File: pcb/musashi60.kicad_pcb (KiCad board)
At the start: 2 copper layers, 175 x 135.7 mm, 81 parts, among them J1 MJ-4PP-9, U1 ProMicro_r

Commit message: update pcb
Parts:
- removed D_H5: D, foostan:D3_TH_SMD
- removed the G_LOGO_B at (79.8, 108.3)
- removed the G_LOGO_F at (79.8, 108.3)
- removed H_D2: MountingHole_Pad, foostan:1pin_conn
- removed SW_H5: SW_PUSH, foostan:CherryMX_Choc_Hotswap
- added G_LOGO_B: LOGO, local:musashi60-silk-256, B.Cu at (90.7, 107.0)
- added G_LOGO_F: LOGO, local:musashi60-silk-256, F.Cu at (89.5, 107.0)
- added SW_RST2: SW_PUSH, foostan:ResetSW_4P, F.Cu at (17.0, 47.6)
- moved JP_RIGHT 128.9 mm to (148.0, 18.0)
- moved JP_LEFT 125.9 mm to (148.0, 18.0)
- moved GND 33.9 mm to (25.4, 48.3)
- moved F5 30.6 mm to (25.4, 45.7)
- moved F4 27.3 mm to (25.4, 43.2)
- moved D3 23.4 mm to (25.4, 40.6)
- moved VCC 20.5 mm to (25.4, 38.1)
- moved D_G5 14.4 mm to (57.5, 119.5), turned to 10 degrees
- moved SW_G5 13.6 mm to (55.8, 110.1), turned to 10 degrees
- moved D_H4 12.4 mm to (36.2, 108.3), turned to 15 degrees
- moved D_G4 11.7 mm to (54.2, 100.7), turned to 10 degrees
- moved D_B1 11.4 mm to (149.5, 42.3)
- moved D_A3 11.3 mm to (168.5, 84.6)
- moved D_F4 11.3 mm to (73.2, 94.8), turned to 5 degrees
- moved D_A4 11.2 mm to (168.4, 103.6)
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- renumbered H_D3 to D3, H_F4 to F4, H_F5 to F5, H_GND1 to GND, H_VCC1 to VCC
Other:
- board size 175 x 135.7 mm -> 185 x 135 mm
- board text added: "Designed by @hamano"
- board text added: "Rev2"

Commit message: update pcb
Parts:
- removed D_G5: D, foostan:D3_TH_SMD
- removed SW_G5: SW_PUSH, foostan:CherryMX_Choc_Hotswap
- moved JP_LEFT 125.2 mm to (22.8, 19.2)
- moved JP_RIGHT 125.2 mm to (22.8, 19.2)
- moved GND 34.7 mm to (44.1, 19.1)
- moved F5 30.6 mm to (40.5, 19.1)
- moved F4 26.7 mm to (36.9, 19.1)
- moved D3 23.0 mm to (33.3, 19.1)
- moved VCC 19.5 mm to (29.8, 19.1)
- moved SW_G4 17.6 mm to (57.2, 108.3), turned to 0 degrees
- moved D_G4 17.4 mm to (57.2, 117.9), turned to 0 degrees
- moved SW_RST1 11.1 mm to (15.5, 50.0)
- moved D_H4 9.98 mm to (33.3, 117.9), turned to 0 degrees
- moved SW_H4 9.13 mm to (33.3, 108.3), turned to 0 degrees
- moved U1 9.04 mm to (32.1, 33.0)
- moved SW_RST2 7.22 mm to (23.8, 50.0), turned to 180 degrees
- moved SW_G2 6.23 mm to (45.4, 60.1), turned to 15 degrees
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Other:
- outline, holes or cut-outs redrawn
- board text added: "Rev3"
- board text removed: "Rev2"

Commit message: update pcb
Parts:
- removed JP_LEFT: Jumper, Jumper:SolderJumper-2_P1.3mm_Open_RoundedPad1.0x1.5mm
- removed SW_RST2: SW_PUSH, foostan:ResetSW_4P
- added D2: MountingHole_Pad, foostan:1pin_conn, F.Cu at (36.8, 17.8)
- added JP_LEFT1: Jumper, Jumper:SolderJumper-2_P1.3mm_Open_RoundedPad1.0x1.5mm, F.Cu at (25.2, 19.2)
- SW_A3, SW_A4, SW_A5, SW_B1, SW_B2, SW_B3, SW_B4, SW_B5, SW_C1, SW_C2, SW_C3, SW_C4, SW_C5, SW_D1, SW_D2, SW_D3, SW_D4, SW_D5, SW_E1, SW_E2, SW_E3, SW_E4, SW_F1, SW_F2, SW_F3, SW_F4, SW_G2, SW_G3, SW_G4, SW_H2, SW_H3, SW_H4: footprint foostan:CherryMX_Choc_Hotswap -> local:CherryMX_Direct_Hotswap_Reversible
- moved D3 6.09 mm to (39.3, 17.8)
- moved F4 5.08 mm to (41.8, 17.8)
- moved VCC1 4.62 mm to (34.2, 17.8)
- moved F5 4.09 mm to (44.4, 17.8)
- moved D_A5 3.75 mm to (178.2, 138.2), turned to 315 degrees
- moved SW_A5 3.59 mm to (183.7, 132.2), turned to 315 degrees
- moved SW_H4 3.42 mm to (33.7, 111.8), turned to 15 degrees
- moved D_D5 3.19 mm to (123.8, 116.5)
- moved GND1 3.13 mm to (46.9, 17.8)
- moved D_H4 3.02 mm to (35.8, 119.6), turned to 15 degrees
- moved D_G4 2.85 mm to (59.7, 116.6)
- moved G_LOGO_F 2.39 mm to (91.7, 109.5)
- moved SW_G4 2.38 mm to (59.5, 108.3)
- moved JP_RIGHT1 2.38 mm to (25.2, 19.2)
- moved SW_D5 2.38 mm to (123.8, 108.3)
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- renumbered GND to GND1, JP_RIGHT to JP_RIGHT1, VCC to VCC1
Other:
- board size 185 x 135 mm -> 185 x 132 mm
- board text added: "Rev5"
- board text removed: "Rev3"

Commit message: update pcb
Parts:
- removed the D_A3 at (169.2, 82.5)
- removed D_H4: D, foostan:D3_TH_SMD
- removed the G_LOGO_B at (91.7, 109.4)
- removed the G_LOGO_F at (91.7, 109.5)
- removed the SW_A3 at (169.7, 74.3)
- removed SW_H4: SW_PUSH, local:CherryMX_Direct_Hotswap_Reversible
- added G_LOGO_B: LOGO, local:musashi60-silk-384, B.Cu at (87.0, 118.0)
- added G_LOGO_F: LOGO, local:musashi60-silk-384, F.Cu at (87.0, 118.0)
- moved SW_RST1 51.8 mm to (56.4, 15.8), turned to 0 degrees
- moved GND1 45.5 mm to (20.0, 54.5)
- moved F5 42.0 mm to (20.0, 51.9)
- moved F4 38.4 mm to (20.0, 49.4)
- moved D3 34.9 mm to (20.0, 46.9)
- moved D2 31.4 mm to (20.0, 44.3)
- moved VCC1 27.9 mm to (20.0, 41.8)
- moved D_A5 18.2 mm to (178.5, 86.8), turned to 80 degrees
- moved D_A1 13.2 mm to (162.9, 35.8), turned to 85 degrees
- moved SW_A5 13.1 mm to (171.4, 81.3)
- moved SW_E4 12.5 mm to (73.0, 100.0)
- moved SW_E1 12.5 mm to (63.1, 44.1)
- moved SW_E2 12.5 mm to (66.3, 62.5)
- moved SW_E3 12.5 mm to (69.6, 81.3)
- moved SW_G2 12.4 mm to (27.5, 81.6)
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- renumbered D_B1 to D_A1, D_B2 to D_A2, D_B3 to D_A3, D_B4 to D_A4, D_A4 to D_A5, D_C1 to D_B1, D_C2 to D_B2, D_C3 to D_B3, D_C4 to D_B4, D_A5 to D_B5, D_D1 to D_C1, D_D2 to D_C2, D_D3 to D_C3, D_D4 to D_C4, D_B5 to D_C5, D_E1 to D_D1, D_E2 to D_D2, D_E3 to D_D3, D_E4 to D_D4, D_C5 to D_D5, D_F1 to D_E1, D_F2 to D_E2, D_F3 to D_E3, D_F4 to D_E4, D_D5 to D_E5, D_G2 to D_F2, D_G3 to D_F3, D_G4 to D_F5, D_H2 to D_G2, D_H3 to D_G3, SW_B1 to SW_A1, SW_B2 to SW_A2, SW_B3 to SW_A3, SW_B4 to SW_A4, SW_A4 to SW_A5, SW_C1 to SW_B1, SW_C2 to SW_B2, SW_C3 to SW_B3, SW_C4 to SW_B4, SW_A5 to SW_B5, SW_D1 to SW_C1, SW_D2 to SW_C2, SW_D3 to SW_C3, SW_D4 to SW_C4, SW_B5 to SW_C5, SW_E1 to SW_D1, SW_E2 to SW_D2, SW_E3 to SW_D3, SW_E4 to SW_D4, SW_C5 to SW_D5, SW_F1 to SW_E1, SW_F2 to SW_E2, SW_F3 to SW_E3, SW_F4 to SW_E4, SW_D5 to SW_E5, SW_G2 to SW_F2, SW_G3 to SW_F3, SW_G4 to SW_F5, SW_H2 to SW_G2, SW_H3 to SW_G3
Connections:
- D_A5 pad 1: B3 -> B2
- D_C3 pad 2: Net-(D_D3-Pad2) (its old number) -> F7
- D_D2 pad 1: F7 -> Net-(D_D2-Pad1)
- D_E2 pad 1: F7 -> Net-(D_D2-Pad1)
- D_F2 pad 1: F7 -> Net-(D_D2-Pad1)
- D_F5 pad 1: B3 -> B2
- D_G2 pad 1: F7 -> Net-(D_D2-Pad1)
- SW_A1 pad 1: D0 -> D1
- SW_A2 pad 1: D0 -> D1
- SW_A3 pad 1: D0 -> D1
- SW_A4 pad 1: D0 -> D1
- SW_B1 pad 1: D4 -> D0
- SW_B2 pad 1: D4 -> D0
- SW_B3 pad 1: D4 -> D0
- SW_B4 pad 1: D4 -> D0
- SW_B5 pad 1: D1 -> D0
- SW_C1 pad 1: C6 -> D4
- SW_C2 pad 1: C6 -> D4
- SW_C3 pad 1: C6 -> D4
- SW_C3 pad 2: Net-(D_D3-Pad2) (its old number) -> F7
- SW_C4 pad 1: C6 -> D4
- SW_C5 pad 1: D0 -> D4
- SW_D1 pad 1: D7 -> C6
- SW_D2 pad 1: D7 -> C6
- SW_D3 pad 1: D7 -> C6
- SW_D4 pad 1: D7 -> C6
- SW_D5 pad 1: D4 -> C6
- SW_E1 pad 1: E6 -> D7
- SW_E2 pad 1: E6 -> D7
- SW_E3 pad 1: E6 -> D7
- SW_E4 pad 1: E6 -> D7
- SW_E5 pad 1: C6 -> D7
- SW_F2 pad 1: B4 -> E6
- SW_F3 pad 1: B4 -> E6
- SW_F5 pad 1: B4 -> E6
- SW_G2 pad 1: B5 -> B4
- SW_G3 pad 1: B5 -> B4
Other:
- board size 185 x 132 mm -> 185 x 130 mm

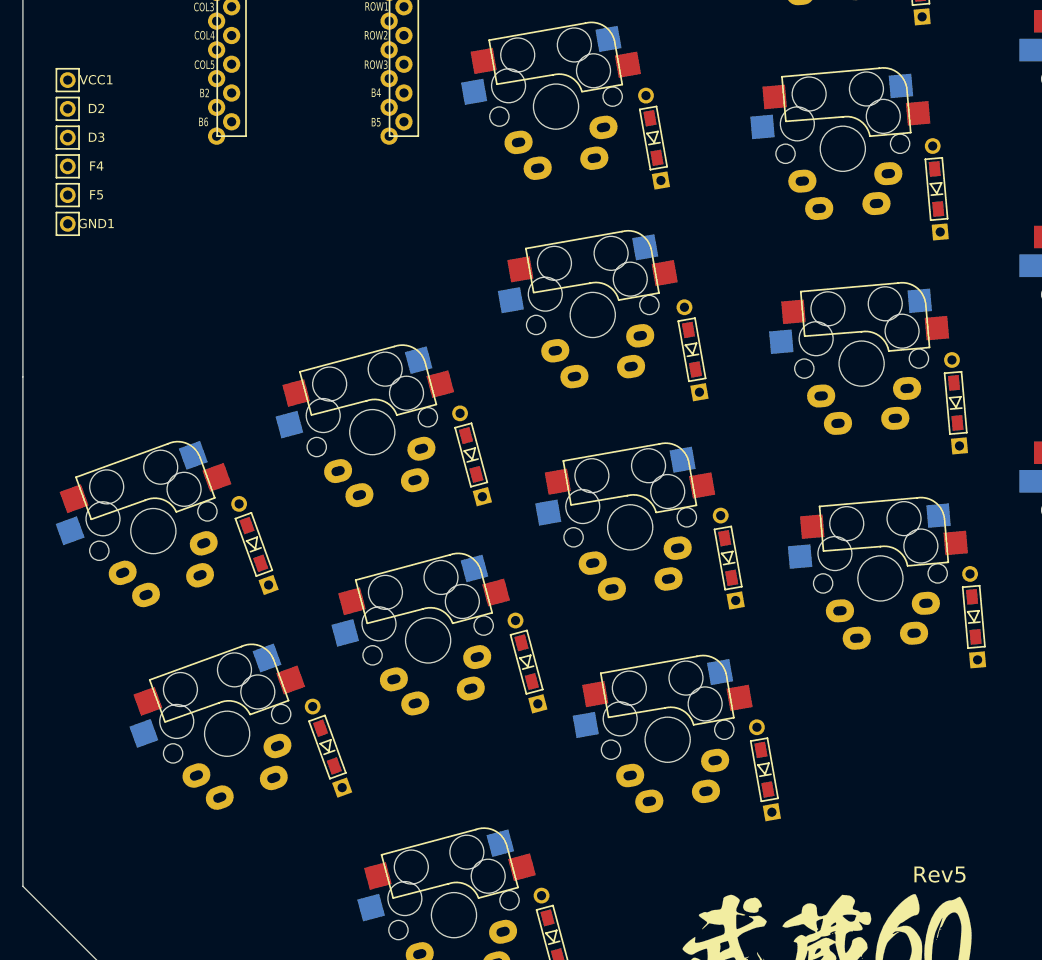
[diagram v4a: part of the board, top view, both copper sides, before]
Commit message: update for rev7 pcb
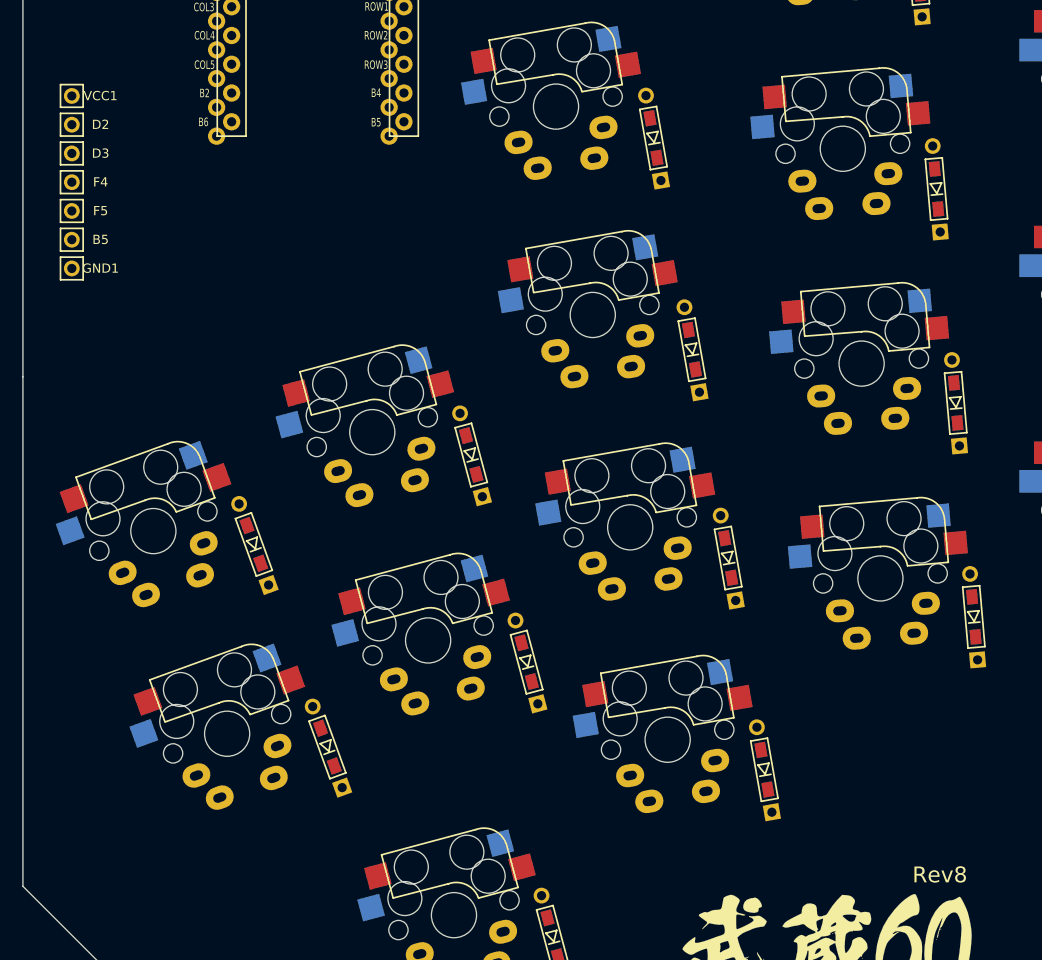
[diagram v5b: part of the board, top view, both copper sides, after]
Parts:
- added B5: MountingHole_Pad, foostan:1pin_conn, F.Cu at (20.3, 55.9)
- moved GND1 3.96 mm to (20.3, 58.4)
- moved F5 1.45 mm to (20.3, 53.3)
- moved D2 1.45 mm to (20.3, 45.7)
- moved D3 1.45 mm to (20.3, 48.3)
- moved F4 1.45 mm to (20.3, 50.8)
- moved VCC1 1.45 mm to (20.3, 43.2)
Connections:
- D_C3 pad 2: F7 -> Net-(D_C3-Pad2)
- D_D2 pad 1: Net-(D_D2-Pad1) -> F7
- D_E2 pad 1: Net-(D_D2-Pad1) -> F7
- D_F2 pad 1: Net-(D_D2-Pad1) -> F7
- D_G2 pad 1: Net-(D_D2-Pad1) -> F7
- SW_C3 pad 2: F7 -> Net-(D_C3-Pad2)
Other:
- board text added: "Rev8"
- board text removed: "Rev5"

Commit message: update pcb for rev8
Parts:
- removed the D_A5 at (178.5, 86.8)
- removed D_F5, D_G3: D, foostan:D3_TH_SMD
- removed F4: MountingHole_Pad, foostan:1pin_conn
- removed the G_LOGO_B at (87.0, 118.0)
- removed the G_LOGO_F at (87.0, 118.0)
- removed the SW_A5 at (171.4, 81.3)
- removed SW_F5, SW_G3: SW_PUSH, local:CherryMX_Direct_Hotswap_Reversible
- added G_LOGO_B: LOGO, local:musashi50-silk-256, B.Cu at (87.0, 113.0)
- added G_LOGO_F: LOGO, local:musashi50-silk-256, F.Cu at (87.0, 113.0)
- added U2: joystick, local:J08K, F.Cu at (173.5, 81.5)
- moved JP_LEFT1 50.2 mm to (74.2, 16.6)
- moved JP_RIGHT1 50.2 mm to (74.2, 16.6)
- moved D3 49.3 mm to (40.8, 93.1)
- moved VCC1 49.3 mm to (40.8, 88.0)
- moved D2 49.3 mm to (40.8, 90.6)
- moved B4 47.2 mm to (40.8, 95.8)
- moved GND1 47.2 mm to (40.8, 100.9)
- moved B5 47.2 mm to (40.8, 98.4)
- moved SW_F2 33.2 mm to (51.0, 58.1), turned to 5 degrees
- moved D_F2 31.3 mm to (59.4, 61.6), turned to 95 degrees
- moved D_A5 11.2 mm to (182.2, 146.4), turned to 45 degrees
- moved SW_E1 11.1 mm to (68.2, 34.3), turned to 5 degrees
- moved SW_A5 10.8 mm to (179.4, 138.0), turned to 315 degrees
- moved D_E1 10.3 mm to (76.5, 37.8), turned to 95 degrees
- moved SW_E2 10.3 mm to (69.8, 52.9), turned to 5 degrees
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- renumbered F5 to B4, D_B5 to D_A5, D_C5 to D_B5, D_D5 to D_C5, D_E5 to D_D5, D_G2 to D_F2, D_F2 to D_F3, D_F3 to D_F4, SW_B5 to SW_A5, SW_C5 to SW_B5, SW_D5 to SW_C5, SW_E5 to SW_D5, SW_G2 to SW_F2, SW_F2 to SW_F3, SW_F3 to SW_F4
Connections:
- B4 pad 1: F5 -> B4
- D_F3 pad 1: F7 -> B1
- D_F4 pad 1: B1 -> B3
- SW_A5 pad 1: D0 -> D1
- SW_B5 pad 1: D4 -> D0
- SW_C5 pad 1: C6 -> D4
- SW_D5 pad 1: D7 -> C6
- SW_F2 pad 1: B4 -> E6
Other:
- board size 185 x 130 mm -> 160 x 140 mm

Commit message: PCBの微調整
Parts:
- moved D_C5 1.02 mm to (152.3, 118.1)
- moved D_D1 0.63 mm to (100.5, 32.1)
- moved D_E2 0.42 mm to (78.2, 56.3)
- moved D_D5 0.36 mm to (132.0, 117.1)
- moved D_B5 0.32 mm to (170.8, 128.2)
- moved D_A5 0.22 mm to (182.1, 146.6)
- moved D_B4 0.13 mm to (138.5, 89.0)
- moved D_C3 0.08 mm to (121.4, 65.4)
- moved D_D2 0.06 mm to (100.5, 51.3)
